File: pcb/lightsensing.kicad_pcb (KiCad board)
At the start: 2 copper layers, 30 x 37 mm, 5 parts, among them Q1 PNP

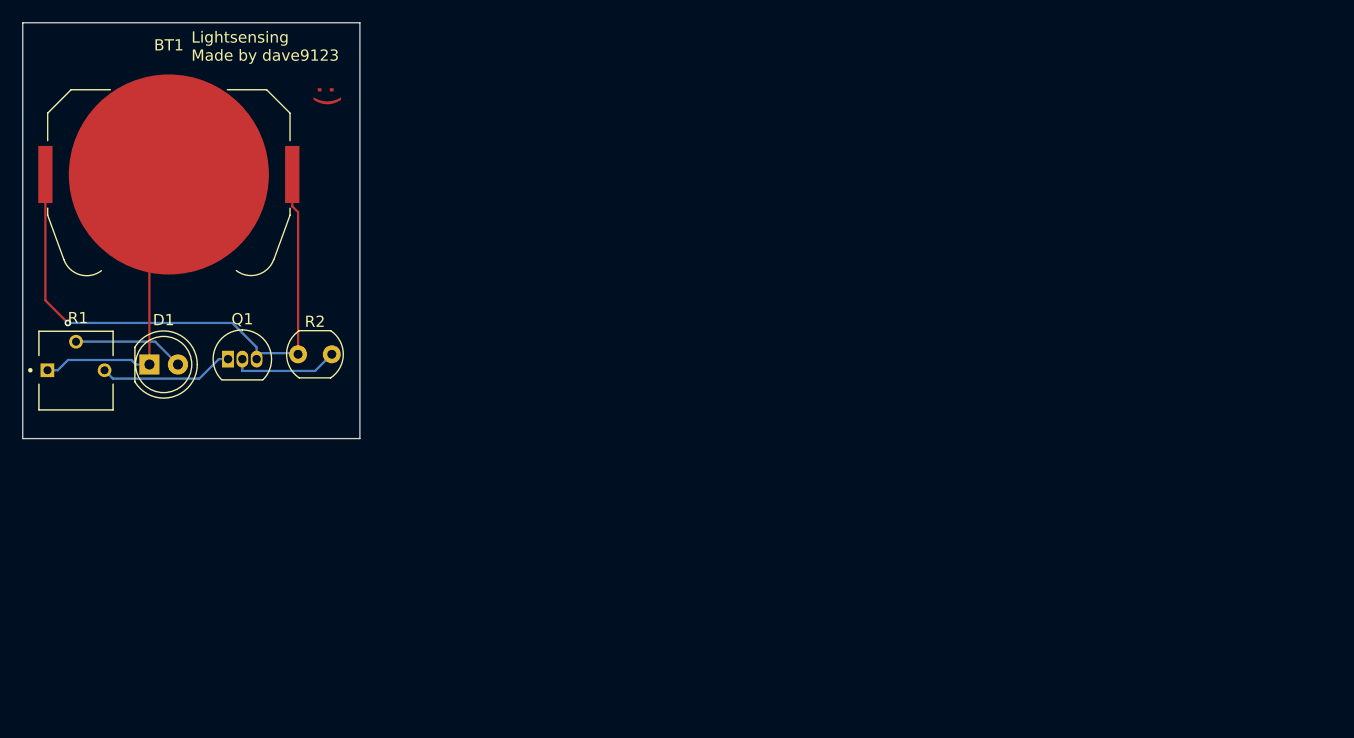
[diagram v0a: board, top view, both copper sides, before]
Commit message: Added some silkscreen and weird looking design
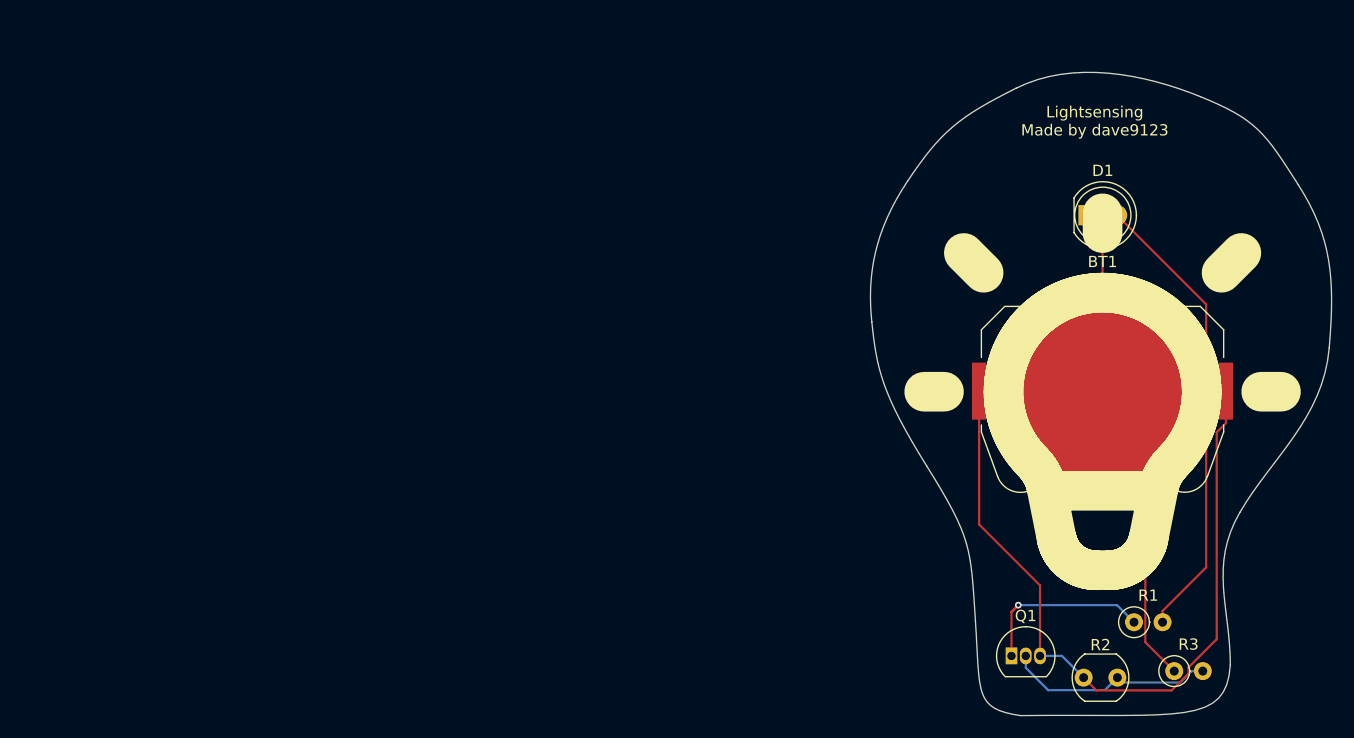
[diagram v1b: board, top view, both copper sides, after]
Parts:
- added R3: 47k, PCM_Resistor_THT_AKL:R_Axial_DIN0207_L6.3mm_D2.5mm_P2.54mm_Vertical, F.Cu at (192.5, 93.2)
- R1: value potentiometer -> 220; footprint pcb:TRIM_3362P-1-103 -> PCM_Resistor_THT_AKL:R_Axial_DIN0207_L6.3mm_D2.5mm_P2.54mm_Vertical
- moved R1 96.8 mm to (188.9, 88.8)
- moved BT1 85.3 mm to (186.1, 68.3)
- moved D1 84.6 mm to (184.8, 52.6)
- moved R2 75.6 mm to (184.4, 93.8)
- moved Q1 74.5 mm to (178.0, 91.8)
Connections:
- R1 pad 1: Net-(BT1--) -> Net-(Q1-C)
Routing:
- net Net-(D1-A): track 9.91 -> 41.1 mm
- net Net-(BT1--): track 27.2 -> 43.7 mm
- net Net-(BT1-+): track 52.7 -> 67.4 mm, vias 1 -> 0
- net Net-(Q1-B): track 9.63 -> 18.7 mm
- net Net-(Q1-C): track 12.0 -> 19.1 mm, vias 0 -> 1
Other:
- board size 30 x 37 mm -> 41 x 57.2 mm
- board text removed: ":)"

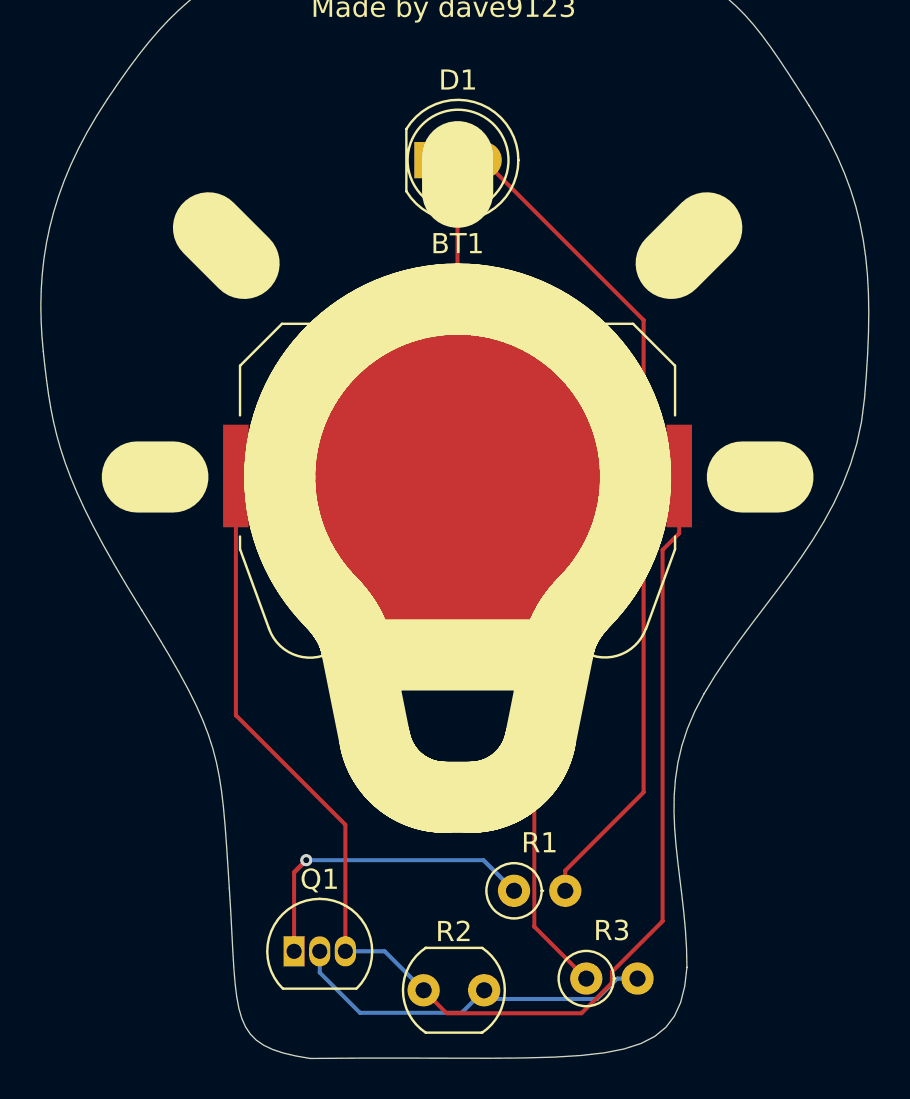
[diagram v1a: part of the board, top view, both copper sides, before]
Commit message: Updated silkscreen
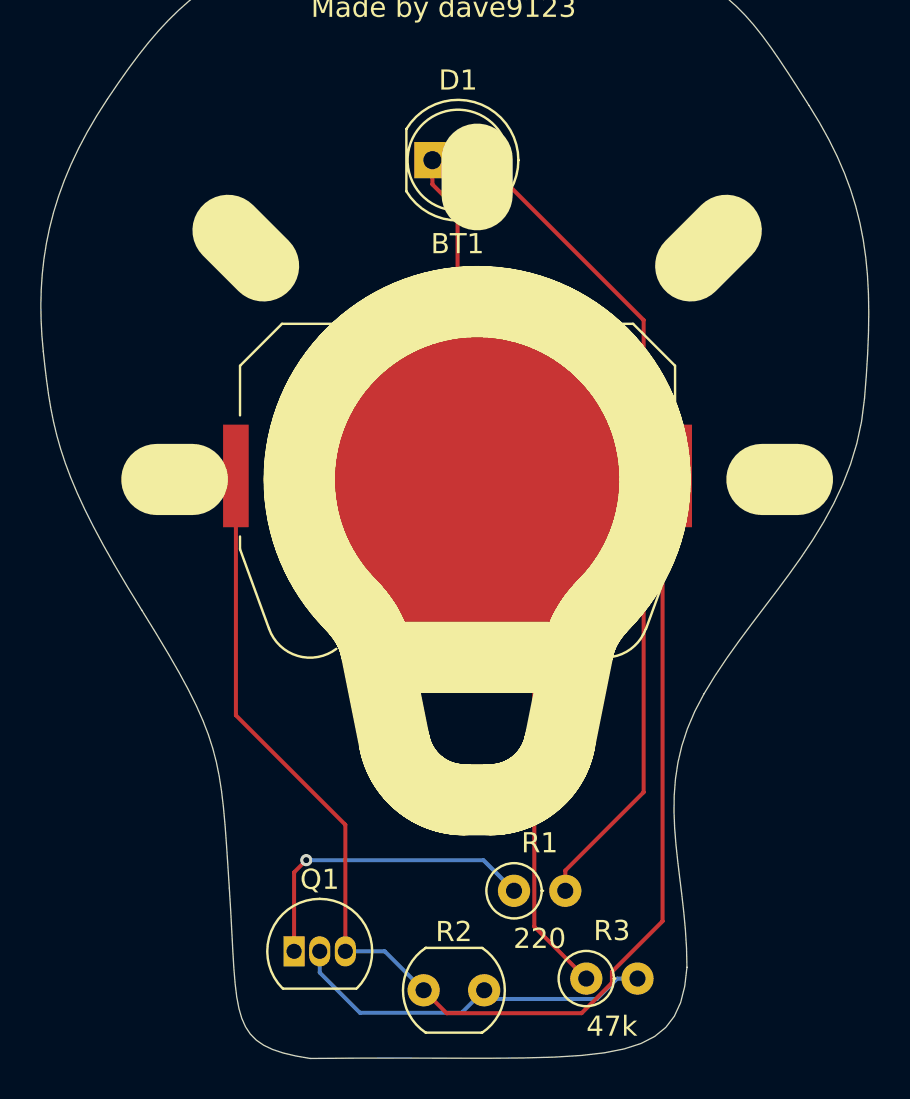
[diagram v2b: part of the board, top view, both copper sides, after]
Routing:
- net Net-(Q1-C): track 19.1 -> 15.7 mm
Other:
- board text added: "Hello"
- board text added: "there :)"
